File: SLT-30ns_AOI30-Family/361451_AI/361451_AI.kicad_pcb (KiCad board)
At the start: 2 copper layers, 12.1 x 12.1 mm, 13 parts, among them T1 T_DB, T2 T_DA, U1 12-Pin_SLx_Can

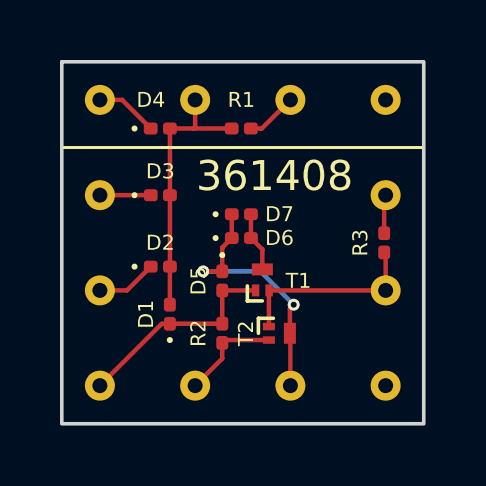
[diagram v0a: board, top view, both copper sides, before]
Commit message: Update schematic pdfs
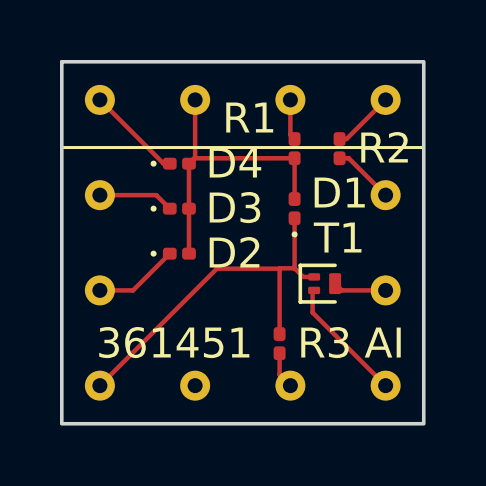
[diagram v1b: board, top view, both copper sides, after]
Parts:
- removed D5, D6, D7: IBM_Diode, Diode_SMD:D_0201_0603Metric
- removed T2: T_DA, Package_DFN_QFN:Diodes_DFN1006-3
- R1: value 1.2K -> 2K
- R2: value 1.8K -> 750Ω
- R3: value 1K -> 3.6K
- T1: value T_DB -> AAA; footprint Package_DFN_QFN:Diodes_DFN1006-3 -> Package_TO_SOT_SMD:SOT-883
- moved R2 7.29 mm to (142.5, 91.0)
- moved D1 5.45 mm to (141.0, 93.0)
- moved R3 4.84 mm to (140.5, 97.5), turned to -90 degrees
- moved T1 2.08 mm to (142.0, 95.5), turned to 0 degrees
- moved R1 1.90 mm to (141.0, 91.0), turned to -90 degrees
- moved D4 1.33 mm to (137.2, 91.5)
- moved D3 0.78 mm to (137.2, 93.0)
- moved D2 0.77 mm to (137.2, 94.5)
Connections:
- R2 pad 1: /1 -> /+3V
- R2 pad 2: GND -> /8
- R3 pad 1: /9 -> /1
- T1 pad 2: /9 -> GND
- T1 pad 3: /7 -> /9
- U1 pad 10: /10 -> GND
- U1 pad 11: /11 -> /-3V
- U1 pad 12: GND -> /12
- U1 pad 7: /7 -> /+3V
- U1 pad 8: /-3V -> /8
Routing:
- net /11: track 8.90 -> 0.00 mm, vias 2 -> 0
- net /1: track 7.15 -> 12.7 mm
- net /9: track 6.45 -> 1.78 mm
- net /+3V: track 0.00 -> 2.08 mm
- net /8: track 0.00 -> 2.04 mm
- net /7: track 2.04 -> 0.00 mm
- net /5: track 8.90 -> 10.2 mm
- net /4: track 2.09 -> 3.21 mm
- net /3: track 1.70 -> 2.52 mm
- net /2: track 2.02 -> 2.84 mm
- net GND: track 3.39 -> 4.20 mm
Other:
- board text added: "361451"
- board text added: "AI"
- board text removed: "361408"
